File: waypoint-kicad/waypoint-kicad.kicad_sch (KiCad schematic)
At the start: 9 parts, among them U1 nRF52840, U2 SX1262IMLTRT, U3 AP2112K-3.3, U4 MCP73831-2-OT, U5 LTC4412xS6, U6 DRV2605LDGS, U7 LIS2DH, U8 LIS2DH

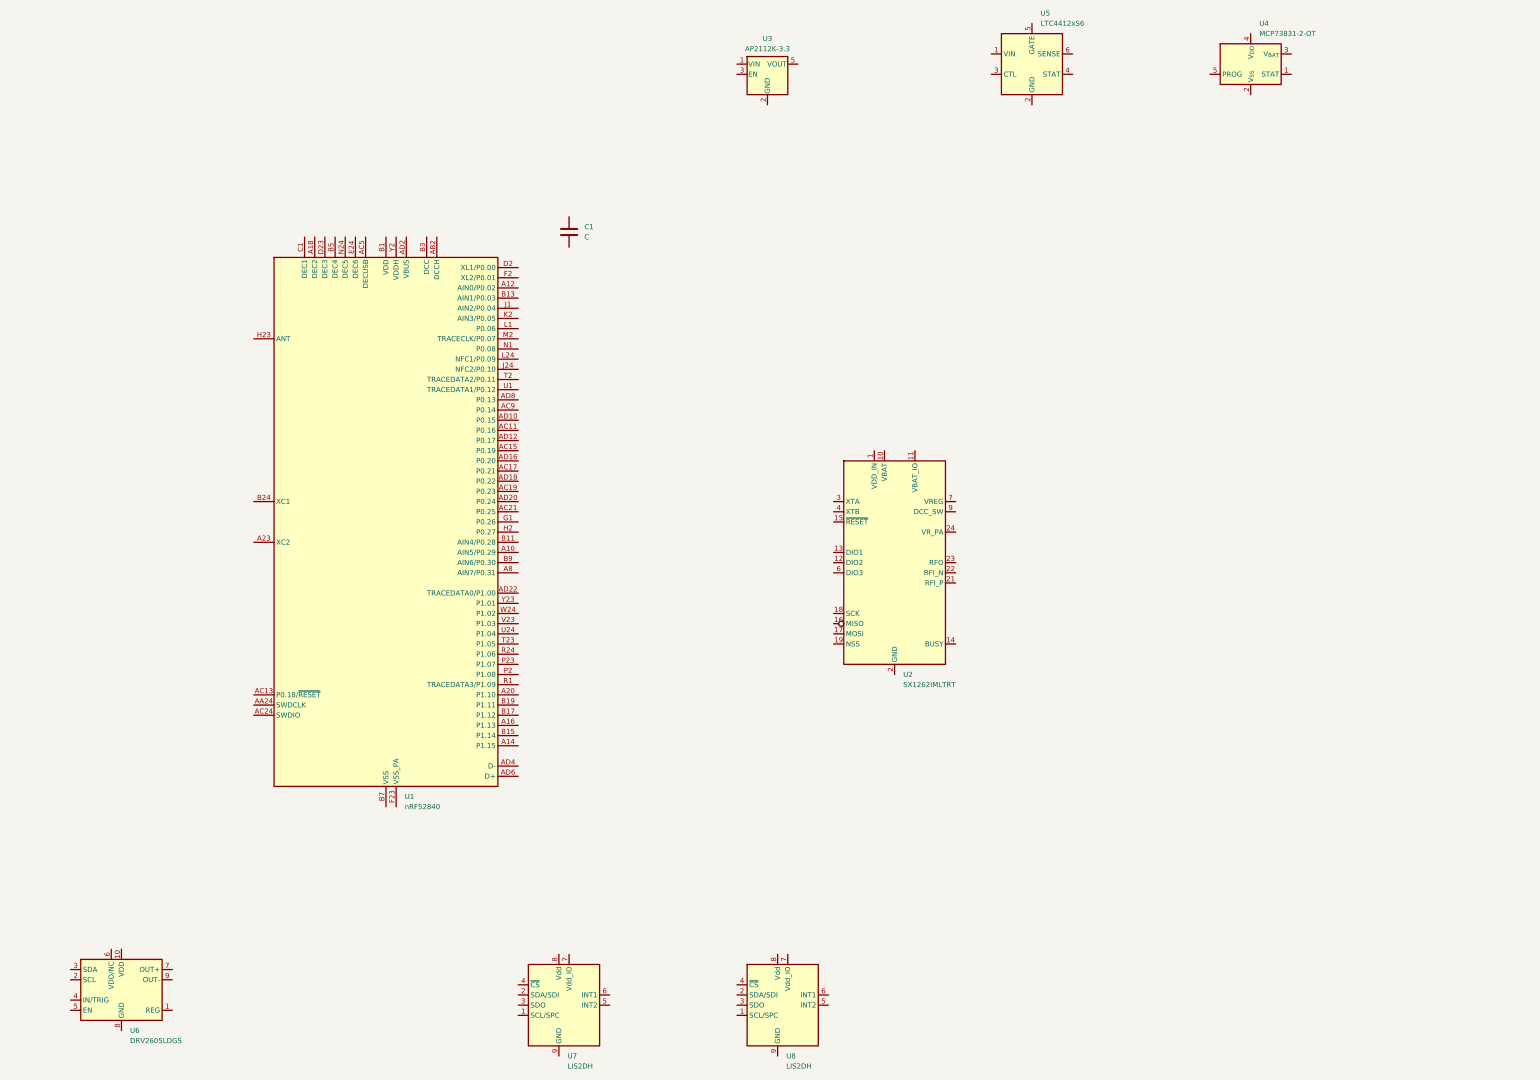
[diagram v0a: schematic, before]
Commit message: Update schematic for waypoint-kicad: rename components and adjust properties
- Renamed capacitor symbol to "Connector:Conn_Coaxial" and updated its properties including reference and value.
- Added new "Connector:TestPoint" symbol with updated properties for test points.
- Introduced "Connector:USB_C_Receptacle_USB2.0_14P" symbol with relevant properties and descriptions.
- Adjusted pin names, offsets, and descriptions for clarity and accuracy.
- Added multiple backup zip files for project versioning.
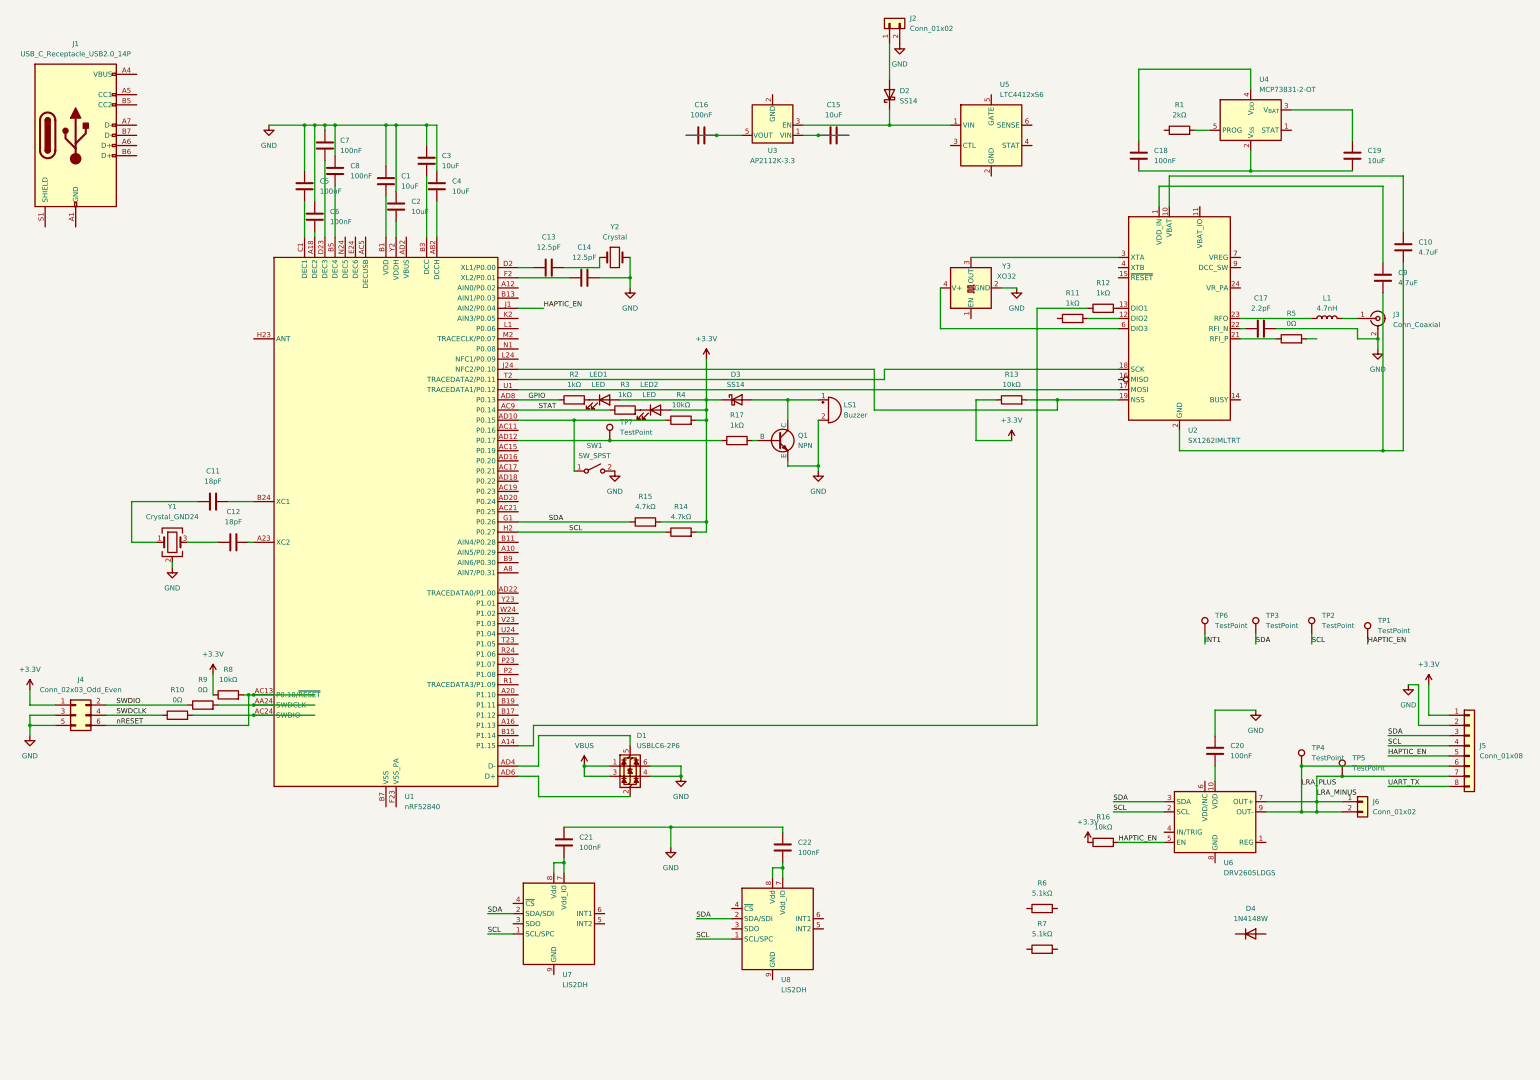
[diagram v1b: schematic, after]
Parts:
- added C10, C9: 4.7uF, Capacitor_SMD:C_0603_1608Metric_Pad1.08x0.95mm_HandSolder, symbol Device:C
- added C11, C12: 18pF, Capacitor_SMD:C_0402_1005Metric_Pad0.74x0.62mm_HandSolder, symbol Device:C
- added C13, C14: 12.5pF, Capacitor_SMD:C_0402_1005Metric_Pad0.74x0.62mm_HandSolder, symbol Device:C
- added C15, C19, C2, C3, C4: 10uF, Capacitor_SMD:C_0805_2012Metric_Pad1.18x1.45mm_HandSolder, symbol Device:C
- added C16, C18, C20, C21, C22, C5, C6, C7, C8: 100nF, Capacitor_SMD:C_0402_1005Metric_Pad0.74x0.62mm_HandSolder, symbol Device:C
- added C17: 2.2pF, Capacitor_SMD:C_0402_1005Metric_Pad0.74x0.62mm_HandSolder, symbol Device:C
- added D1: USBLC6-2P6, Package_TO_SOT_SMD:SOT-666, symbol Power_Protection:USBLC6-2P6
- added D2, D3: SS14, Diode_SMD:D_SMA, symbol Diode:SS14
- added D4: 1N4148W, Diode_SMD:D_SOD-123, symbol Diode:1N4148W
- added J1: USB_C_Receptacle_USB2.0_14P, symbol Connector:USB_C_Receptacle_USB2.0_14P
- added J2, J6: Conn_01x02, symbol Connector_Generic:Conn_01x02
- added J3: Conn_Coaxial, symbol Connector:Conn_Coaxial
- added J4: Conn_02x03_Odd_Even, symbol Connector_Generic:Conn_02x03_Odd_Even
- added J5: Conn_01x08, symbol Connector_Generic:Conn_01x08
- added L1: 4.7nH, symbol Device:L
- added LED1, LED2: LED, LED_SMD:LED_0805_2012Metric, symbol Device:LED
- added LS1: Buzzer, Buzzer_Beeper:Buzzer_CUI_CPT-9019S-SMT, symbol Device:Buzzer
- added Q1: NPN, symbol Simulation_SPICE:NPN
- added R1: 2kΩ, Resistor_SMD:R_0402_1005Metric_Pad0.72x0.64mm_HandSolder, symbol Device:R
- added R10, R5, R9: 0Ω, Resistor_SMD:R_0402_1005Metric_Pad0.72x0.64mm_HandSolder, symbol Device:R
- added R11, R12, R17, R2, R3: 1kΩ, Resistor_SMD:R_0402_1005Metric_Pad0.72x0.64mm_HandSolder, symbol Device:R
- added R13, R16, R4, R8: 10kΩ, Resistor_SMD:R_0402_1005Metric_Pad0.72x0.64mm_HandSolder, symbol Device:R
- added R14, R15: 4.7kΩ, Resistor_SMD:R_0402_1005Metric_Pad0.72x0.64mm_HandSolder, symbol Device:R
- added R6, R7: 5.1kΩ, Resistor_SMD:R_0603_1608Metric_Pad0.98x0.95mm_HandSolder, symbol Device:R
- added SW1: SW_SPST, Button_Switch_SMD:SW_SPST_Omron_B3FS-105xP, symbol Switch:SW_SPST
- added TP1, TP2, TP3, TP4, TP5, TP6, TP7: TestPoint, symbol Connector:TestPoint
- added Y1: Crystal_GND24, Crystal:Crystal_SMD_2016-4Pin_2.0x1.6mm, symbol Device:Crystal_GND24
- added Y2: Crystal, Crystal:Crystal_SMD_3215-2Pin_3.2x1.5mm, symbol Device:Crystal
- added Y3: XO32, Oscillator:Oscillator_SMD_EuroQuartz_XO32-4Pin_3.2x2.5mm, symbol Oscillator:XO32
- C1: value C -> 10uF; footprint (none) -> Capacitor_SMD:C_0805_2012Metric_Pad1.18x1.45mm_HandSolder
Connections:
- net at U4.2 (V_{SS}): now also C18.1, C19.1
- net at U4.3 (V_{BAT}): now also C19.2
- net at U4.4 (V_{DD}): now also C18.2
- net at U4.5 (PROG): now also R1.2
- net at U2.1 (VDD_IN): now also C9.1
- net at U2.10 (VBAT): now also C10.1
- net at U2.12 (DIO2): now also R11.2
- net at U2.13 (DIO1): now also R12.2
- net at U2.17 (MOSI): now also U1.U1 (TRACEDATA1/P0.12)
- net at U2.18 (SCK): now also U1.T2 (TRACEDATA2/P0.11)
- net at U2.19 (NSS): now also U1.J24 (NFC2/P0.10), R13.2
- net at U2.2 (GND), U2.20 (GND), U2.25 (GND)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: now also C10.2, C9.2
- net at U2.21 (RFI_P): now also R5.1
- net at U2.22 (RFI_N): now also C17.1
- net at U2.23 (RFO): now also L1.1
- net at U2.3 (XTA): now also Y3.3 (OUT)
- net at U2.6 (DIO3): now also Y3.4 (V+)
- net at U6.10 (VDD): now also C20.1
- net SCL: now reaches U6.2 (SCL)
- net SCL: now also U1.H2 (P0.27), U7.1 (SCL/SPC), U8.1 (SCL/SPC), J5.4 (Pin_4), R14.1, TP2.1
- net SDA: now reaches U6.3 (SDA)
- net SDA: now also U1.G1 (P0.26), U7.2 (SDA/SDI), U8.2 (SDA/SDI), J5.3 (Pin_3), R15.1, TP3.1
- net HAPTIC_EN: now reaches U6.5 (EN)
- net HAPTIC_EN: now also U1.J1 (AIN2/P0.04), J5.5 (Pin_5), R16.2, TP1.1
- net LRA_MINUS: now reaches U6.7 (OUT+)
- net LRA_MINUS: now also U6.9 (OUT-), J5.6 (Pin_6), J5.7 (Pin_7), J6.1 (Pin_1), J6.2 (Pin_2), TP4.1, TP5.1
- net at U8.7 (Vdd_IO): now also U8.8 (Vdd), C22.1
- net at U3.1 (VIN): now also C15.1, C15.2
- net at U3.3 (EN): now also U5.1 (VIN), D2.1 (K)
- net at U3.5 (VOUT): now also C16.1, C16.2
- net at U7.7 (Vdd_IO): now also U7.8 (Vdd), C21.1
- net at U1.A14 (P1.15): now also R12.1
- net at U1.A18 (DEC2): now also C6.2
- net at U1.A22 (VDD), U1.AD14 (VDD), U1.AD23 (VDD)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: now also C1.2
- net at U1.A23 (XC2): now also C12.2
- net at U1.AA24 (SWDCLK): now also R9.2
- net at U1.AB2 (DCCH): now also C4.2
- net nRESET: now reaches U1.AC13 (P0.18/~{RESET})
- net nRESET: now also J4.6 (Pin_6), R8.2
- net at U1.AC24 (SWDIO): now also R10.2
- net STAT: now reaches U1.AC9 (P0.14)
- net STAT: now also R3.1
- net at U1.AD10 (P0.15): now also R4.1, SW1.1 (A)
- net at U1.AD12 (P0.17): now also R17.1, TP7.1
- net at U1.AD4 (D-): now also D1.5 (VBUS)
- net at U1.AD6 (D+): now also D1.2 (GND)
- net GPIO: now reaches U1.AD8 (P0.13)
- net GPIO: now also R2.1
- net at U1.B24 (XC1): now also C11.2
- net at U1.B3 (DCC): now also C3.2
- net at U1.B5 (DEC4): now also C8.2
- net at U1.C1 (DEC1): now also C5.2
- net at U1.D2 (XL1/P0.00): now also C13.1
- net at U1.D23 (DEC3): now also C7.2
- net at U1.F2 (XL2/P0.01): now also C14.1
- net at U1.Y2 (VDDH): now also C2.2
- net GND: now reaches C1.1
- net GND: now also C14.2, C17.2, C2.1, C20.2, C21.2, C22.2, C3.1, C4.1, C5.1, C6.1, C7.1, C8.1, D1.4 (I/O2), D1.6 (I/O1), J2.2 (Pin_2), J3.2 (Ext), J4.3 (Pin_3), J4.5 (Pin_5), J5.2 (Pin_2), LS1.2 (-), Q1.3 (E), SW1.2 (B), Y1.2 (G), Y1.4 (G), Y2.2, Y3.2 (GND)
- new net: J3.1 (In), L1.2
- new net: D2.2 (A), J2.1 (Pin_1)
- new net: C13.2, Y2.1
- new net: D3.2 (A), LS1.1 (+), Q1.1 (C)
- new net: Q1.2 (B), R17.2
- new net: LED2.1 (K), R3.2
- new net: C11.1, Y1.1
- new net: LED1.1 (K), R2.2
- new net: C12.1, Y1.3
- new net: J1.A1 (GND), J1.A12 (GND), J1.B1 (GND), J1.B12 (GND)
- new net: J1.A4 (VBUS), J1.A9 (VBUS), J1.B4 (VBUS), J1.B9 (VBUS)
- new net +3.3V: D3.1 (K), J4.1 (Pin_1), J5.1 (Pin_1), LED1.2 (A), LED2.2 (A), R13.1, R14.2, R15.2, R16.1, R4.2, R8.1
- new net INT1: TP6.1
- new net SWDCLK: J4.4 (Pin_4), R10.1
- new net SWDIO: J4.2 (Pin_2), R9.1
- new net UART_TX: J5.8 (Pin_8)
- new net VBUS: D1.1 (I/O1), D1.3 (I/O2)
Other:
- moved on the sheet: C1, U2, U3, U4, U5, U6, U7, U8

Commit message: Update waypoint-kicad files: refine component placements and documentation
- Updated .gitignore to exclude log files and backup directories.
- Revised BOM with pricing to correct resistor placements and clarify component usage.
- Adjusted component placement guide to reflect changes in IC references and configurations.
- Added future improvements document outlining potential enhancements and cost optimizations for the project.
- Updated design specification to include new capacitor and resistor details, ensuring accurate pin assignments and connections.
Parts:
- removed D4: 1N4148W, Diode_SMD:D_SOD-123, symbol Diode:1N4148W
- removed R17: 1kΩ, Resistor_SMD:R_0402_1005Metric_Pad0.72x0.64mm_HandSolder, symbol Device:R
- removed U5: LTC4412xS6, Package_TO_SOT_SMD:TSOT-23-6, symbol Power_Management:LTC4412xS6
- removed U8: LIS2DH, Package_LGA:LGA-14_2x2mm_P0.35mm_LayoutBorder3x4y, symbol Sensor_Motion:LIS2DH
- added C23, C24, C25: 100nF, Capacitor_SMD:C_0402_1005Metric_Pad0.74x0.62mm_HandSolder, symbol Device:C
- added C26: 4.7uF, Capacitor_SMD:C_0603_1608Metric_Pad1.08x0.95mm_HandSolder, symbol Device:C
- C22: value 100nF -> 4.7uF; footprint Capacitor_SMD:C_0402_1005Metric_Pad0.74x0.62mm_HandSolder -> Capacitor_SMD:C_0603_1608Metric_Pad1.08x0.95mm_HandSolder
- TP4: value TestPoint -> TP_LRA_PLUS
- TP5: value TestPoint -> TP_LRA_MINUS
- renumbered U6 to U5, U7 to U6
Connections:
- net INT1 is gone; now on net ACCEL1_INT1: TP6.1
- net +3.3V: now also C1.1, C1.2, C10.1, C10.2, C13.2, C14.2, C15.1, C15.2, C16.1, C16.2, C17.2, C18.1, C19.1, C2.1, C2.2, C20.1, C20.2, C21.1, C21.2, C22.2, C3.1, C4.1, C5.1, C6.1, C7.1, C8.1, C9.1, C9.2, D1.2 (GND), J1.A1 (GND), J1.A12 (GND), J1.B1 (GND), J1.B12 (GND), J1.S1 (SHIELD), J2.2 (Pin_2), J3.2 (Ext), J4.3 (Pin_3), J4.5 (Pin_5), J5.2 (Pin_2), LS1.2 (-), Q1.3 (E), R1.1, R6.2, R7.2, SW1.2 (B), U1.A22 (VDD), U1.AD14 (VDD), U1.AD23 (VDD), U1.B1 (VDD), U1.B7 (VSS), U1.EP (VSS), U1.F23 (VSS_PA), U1.W1 (VDD), U1.Y2 (VDDH), U2.1 (VDD_IN), U2.10 (VBAT), U2.11 (VBAT_IO), U2.2 (GND), U2.20 (GND), U2.25 (GND), U2.5 (GND), U2.8 (GND), U3.2 (GND), U3.3 (EN), U3.5 (VOUT), U4.2 (V_{SS}), U5.10 (VDD), U5.8 (GND), U6.10 (GND), U6.11 (GND), U6.12 (GND), U6.13 (GND), U6.14 (GND), U6.4 (~{CS}), U6.7 (Vdd_IO), U6.8 (Vdd), U6.9 (GND), Y1.2 (G), Y1.4 (G), Y3.2 (GND), Y3.4 (V+), C23.2, C24.1, C25.1, C26.2
- net LRA_MINUS: no longer J5.6 (Pin_6), J6.1 (Pin_1), TP4.1, U5.7 (OUT+)
- net VBUS: now also C18.2, D1.5 (VBUS), D2.2 (A), J1.A4 (VBUS), J1.A9 (VBUS), J1.B4 (VBUS), J1.B9 (VBUS), J2.1 (Pin_1), U4.4 (V_{DD}); no longer D1.1 (I/O1), D1.3 (I/O2)
- net at J3.1 (In), L1.2: now also R5.2
- net LORA_DIO1_SX: now reaches R12.1, U1.A14 (P1.15)
- net USB_CC2: now reaches R7.1
- net USB_CC2: now also J1.B5 (CC2)
- net at Y2.1: now also C14.1, U1.F2 (XL2/P0.01); no longer C13.2
- net at Q1.2 (B): now also R11.2
- net VBAT: now reaches C19.2, U4.3 (V_{BAT})
- net VBAT: now also D2.1 (K), U3.1 (VIN)
- net at U2.12 (DIO2): no longer R11.2
- net LORA_BUSY: now reaches U2.14 (BUSY)
- net LORA_BUSY: now also U1.B15 (P1.14)
- net LORA_RESET: now reaches U2.15 (~{RESET})
- net LORA_RESET: now also U1.R24 (P1.06)
- net SPI_MISO: now reaches U2.16 (MISO)
- net SPI_MISO: now also U1.A16 (P1.13)
- net at U1.U1 (TRACEDATA1/P0.12): no longer U2.17 (MOSI)
- net at U1.T2 (TRACEDATA2/P0.11): no longer U2.18 (SCK)
- net SPI_NSS: now reaches R13.2, U2.19 (NSS)
- net SPI_NSS: now also U1.A20 (P1.10); no longer U1.J24 (NFC2/P0.10)
- net at U2.24 (VR_PA): now also C23.1
- net at U2.6 (DIO3): now also Y3.1 (EN); no longer Y3.4 (V+)
- net at U2.7 (VREG): now also C22.1
- net at TP7.1, U1.AD12 (P0.17): now also R11.1
- net USB_CC1: now reaches R6.1
- net USB_CC1: now also J1.A5 (CC1)
- net at C13.1, U1.D2 (XL1/P0.00): now also Y2.2
- net USB_DP: now reaches U1.AD6 (D+)
- net USB_DP: now also D1.1 (I/O1), D1.6 (I/O1), J1.A6 (D+), J1.B6 (D+); no longer D1.2 (GND)
- net USB_DM: now reaches U1.AD4 (D-)
- net USB_DM: now also D1.3 (I/O2), D1.4 (I/O2), J1.A7 (D-), J1.B7 (D-); no longer D1.5 (VBUS)
- net ACCEL1_INT1: now reaches U6.6 (INT1)
- net at U1.AC5 (DECUSB): now also C26.1
- net SPI_MOSI: now reaches U1.B17 (P1.12)
- net SPI_MOSI: now also U2.17 (MOSI)
- net SPI_SCK: now reaches U1.B19 (P1.11)
- net SPI_SCK: now also U2.18 (SCK)
- net at U1.E24 (DEC6): now also C25.2
- net at U1.N24 (DEC5): now also C24.2
- removed net GND: C1.1, C14.2, C17.2, C2.1, C20.2, C21.2, C22.2, C3.1, C4.1, C5.1, C6.1, C7.1, C8.1, D1.4 (I/O2), D1.6 (I/O1), J2.2 (Pin_2), J3.2 (Ext), J4.3 (Pin_3), J4.5 (Pin_5), J5.2 (Pin_2), LS1.2 (-), Q1.3 (E), SW1.2 (B), Y1.2 (G), Y1.4 (G), Y2.2, Y3.2 (GND)
- new net LRA_PLUS: J5.6 (Pin_6), J6.1 (Pin_1), TP4.1, U5.7 (OUT+)
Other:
- note added: "DIO2 - NC (no antenna switch)"
- moved on the sheet: C1, C10, C13, C14, C15, C16, C18, C19, C2, C20, C21, C3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
